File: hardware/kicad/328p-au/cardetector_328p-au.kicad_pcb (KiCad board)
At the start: 2 copper layers, 64 parts, among them IC1 ATMEGA328-A, K1 RELAY_1RT, P1 RELAY OUT, P2 ISP, P3 TTL OUT, P4 LOOP, P5 I2C, Q1 BC817-40, Q2 BC817-40, Q3 BSS138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

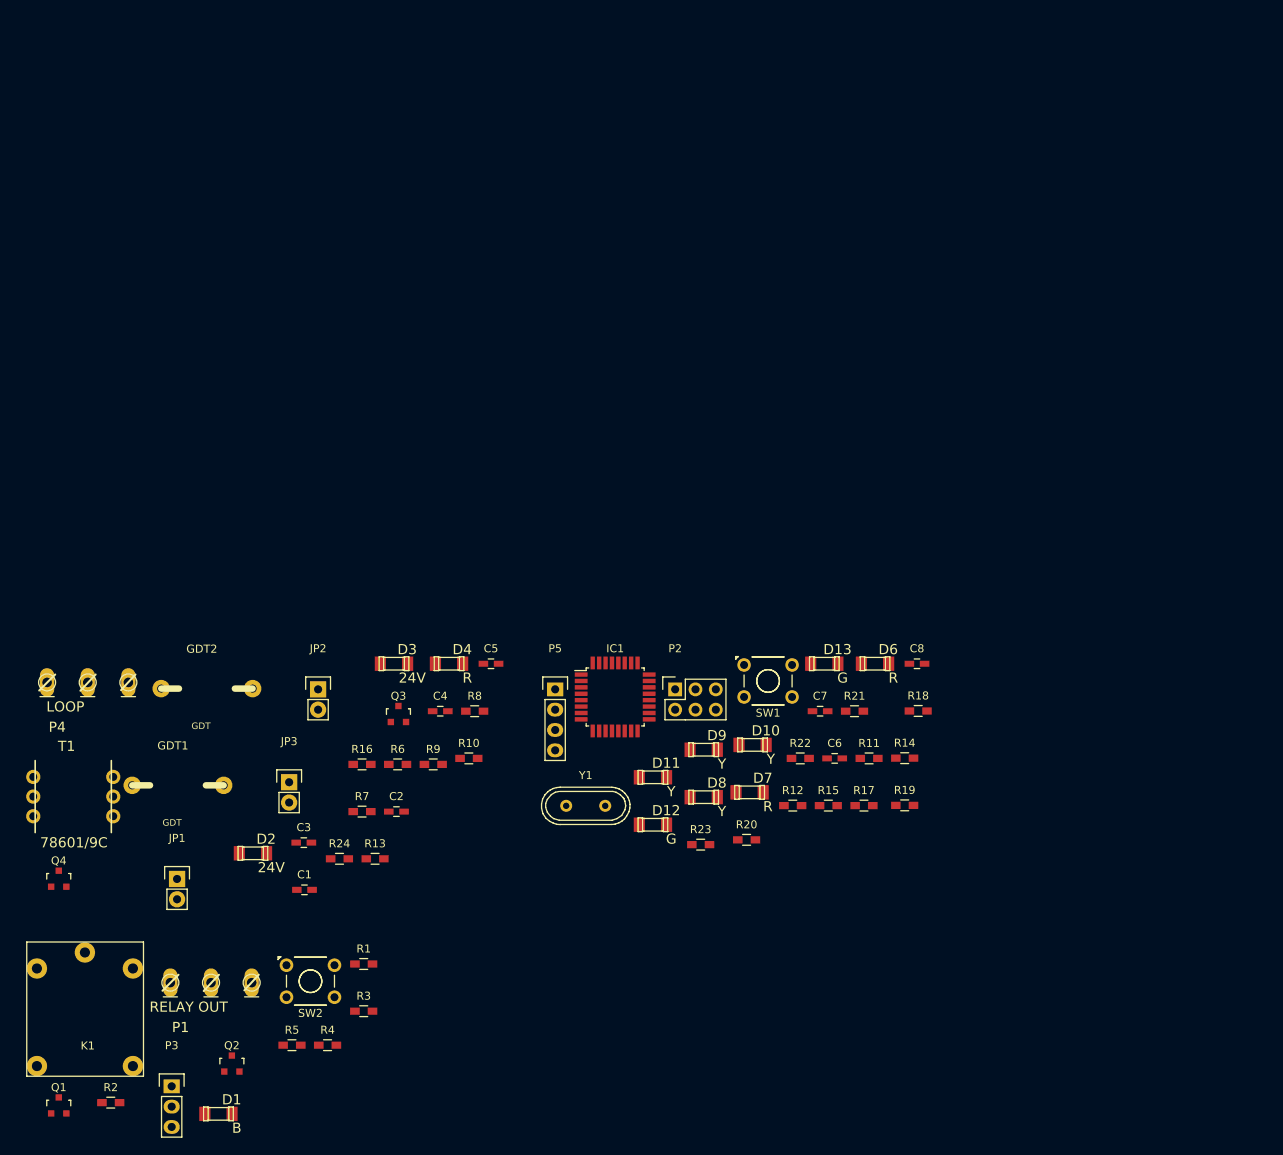
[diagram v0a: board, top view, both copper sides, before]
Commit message: hardware/kicad/328p-au: use 3x2 jumper block for frequency selection
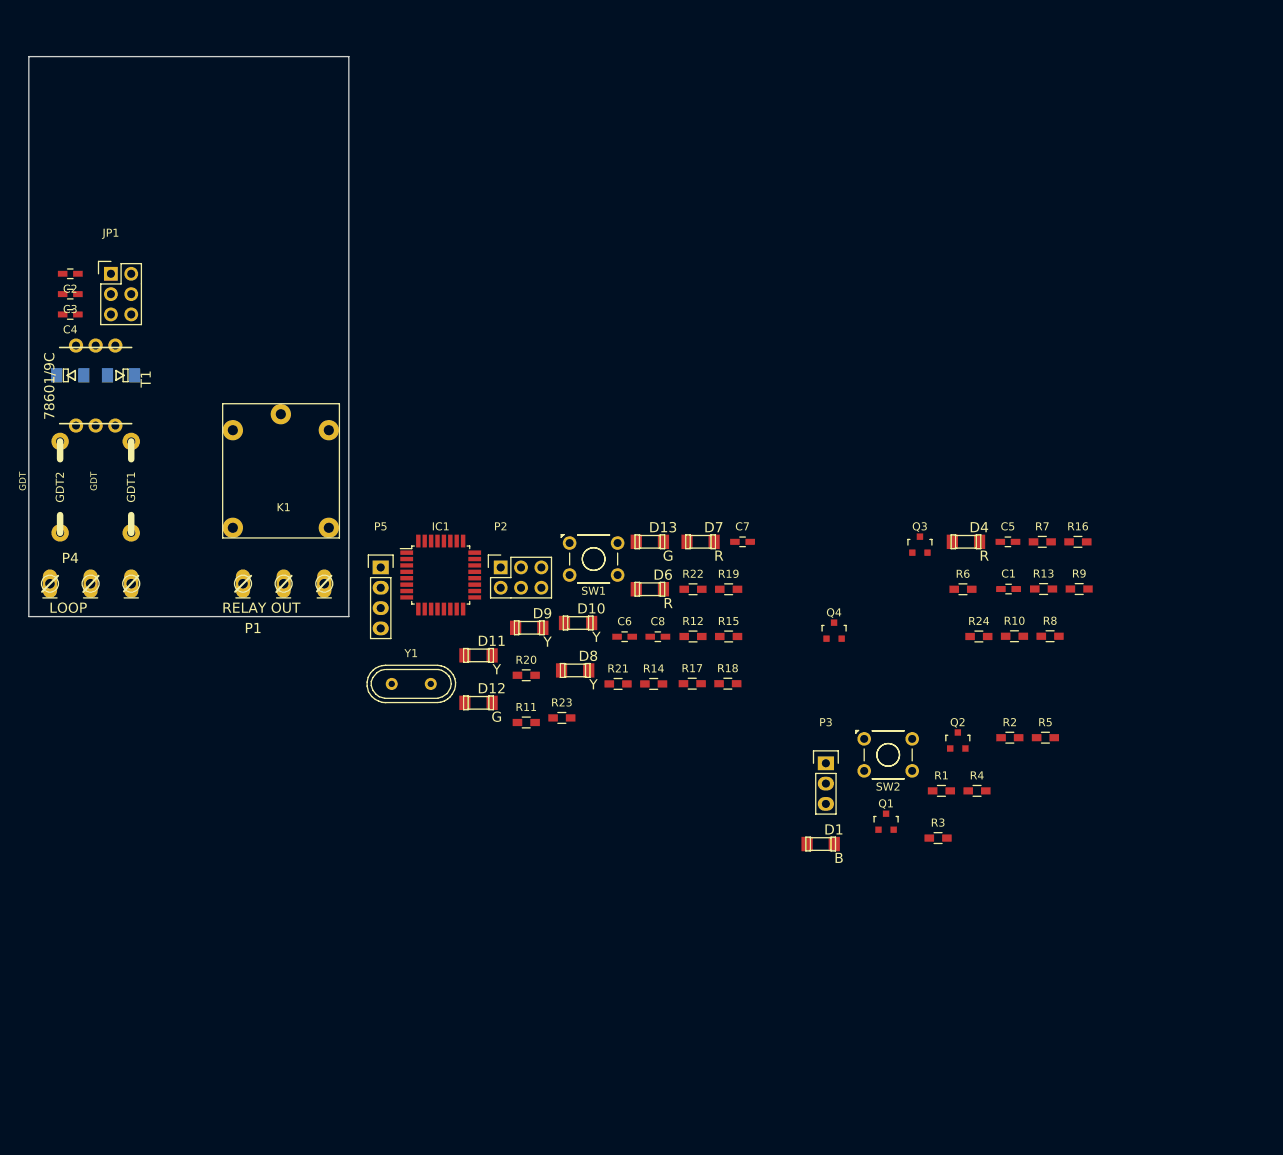
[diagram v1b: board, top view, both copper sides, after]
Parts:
- removed JP2, JP3: Jumper_NO_Small, Pin_Headers:Pin_Header_Straight_1x02
- D2, D3: moved to B.Cu
- JP1: value Jumper_NO_Small -> JP3x2; footprint Pin_Headers:Pin_Header_Straight_1x02 -> Pin_Headers:Pin_Header_Straight_2x03
- moved R2 121.3 mm to (287.6, 115.1)
- moved Q1 109.3 mm to (272.2, 125.6)
- moved Q4 101.8 mm to (265.7, 101.8)
- moved R5 101.7 mm to (292.1, 115.1)
- moved Q2 99.3 mm to (281.1, 115.5)
- moved C1 95.7 mm to (287.5, 96.6)
- moved R16 93.7 mm to (296.1, 90.7)
- moved R7 91.5 mm to (291.7, 90.7)
- moved P3 91.2 mm to (264.6, 118.3)
- moved R13 90.1 mm to (291.8, 96.6)
- moved R4 87.2 mm to (283.5, 121.8)
- moved R24 84.6 mm to (283.8, 102.5)
- moved R9 83.7 mm to (296.3, 96.6)
- moved D1 82.5 mm to (264.0, 128.4)
- moved C2 78.6 mm to (170.2, 57.1), turned to 180 degrees
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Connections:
- JP1 pad 1: Net-(D3-Pad2) -> Net-(C2-Pad1)
- JP1 pad 2: Net-(C2-Pad1) -> Net-(D3-Pad2)
- P1 pad 1: Net-(K1-Pad4) -> Net-(K1-Pad3)
- P1 pad 3: Net-(K1-Pad3) -> Net-(K1-Pad4)
- T1 pad 1: Net-(GDT1-Pad1) -> Net-(C1-Pad1)
- T1 pad 3: Net-(GDT1-Pad2) -> Net-(D3-Pad2)
- T1 pad 4: Net-(D3-Pad2) -> Net-(GDT1-Pad2)
- T1 pad 6: Net-(C1-Pad1) -> Net-(GDT1-Pad1)
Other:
- board outline added: 40 x 70 mm

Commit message: hardware/kicad: added serial connector && 3 push buttons
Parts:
- added P6: CONN_01X03, Pin_Headers:Pin_Header_Straight_1x03, F.Cu at (232.6, 74.8)
- added SW3: TACTILE_SW, Buttons_Switches_ThroughHole:SW_TH_Tactile_Omron_B3F-10xx, F.Cu at (239.2, 81.5)
- added SW4: TACTILE_SW, Buttons_Switches_ThroughHole:SW_TH_Tactile_Omron_B3F-10xx, F.Cu at (248.2, 82.5)
- added SW5: TACTILE_SW, Buttons_Switches_ThroughHole:SW_TH_Tactile_Omron_B3F-10xx, F.Cu at (236.1, 91.6)
- moved R23 64.7 mm to (281.6, 71.6)
- moved Q1 64.1 mm to (307.1, 72.0)
- moved R1 63.5 mm to (318.1, 71.6)
- moved D12 62.5 mm to (269.9, 71.6)
- moved R4 58.5 mm to (313.6, 71.6)
- moved D8 55.5 mm to (276.2, 71.6)
- moved R11 51.0 mm to (268.6, 83.5)
- moved SW2 50.7 mm to (295.4, 71.8)
- moved P3 50.7 mm to (290.6, 74.8)
- moved R3 50.7 mm to (304.6, 84.2)
- moved D1 50.7 mm to (290.0, 84.9)
- moved D9 48.6 mm to (269.9, 77.5)
- moved Y1 46.5 mm to (243.5, 73.5)
- moved R21 46.0 mm to (277.2, 83.4)
- moved C8 43.8 mm to (279.6, 77.5)
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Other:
- board size 40 x 70 mm -> 40 x 75 mm
